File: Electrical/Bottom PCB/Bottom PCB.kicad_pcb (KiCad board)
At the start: 2 copper layers, 100 x 80 mm, 39 parts, among them J1 Steper1, J10 Servo4, J2 Steper2, J3 H Bridge, J4 4 x OP, J6 Servo1, J7 Servo2, J8 Servo3, J9 MainIO, SW1 FL, SW2 FR, U1 ULN2003A, U2 74HC595, U3 QRE1113, U4 TB6612FNG, U5 74HC595, U6 QRE1113, U7 QRE1113, U8 QRE1113

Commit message: updates
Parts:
- moved J1 3.70 mm to (126.0, 111.0)
- moved U1 3.42 mm to (144.0, 119.5)
- moved J2 2.97 mm to (130.0, 111.0)
- moved J6 2.23 mm to (131.5, 75.2)
- moved J10 1.70 mm to (124.0, 75.2)
- moved J7 0.92 mm to (129.0, 75.2)
- moved J8 0.39 mm to (126.5, 75.2)
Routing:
- net Servo4: track 37.6 -> 0.00 mm
- net Servo2: track 32.7 -> 2.00 mm
- net Servo1: track 30.3 -> 0.00 mm
- net +5V: track 142.1 -> 117.3 mm
- net Servo3: track 24.1 -> 0.00 mm
- net DATA: track 20.3 -> 2.14 mm
- net SRCLK: track 37.0 -> 19.8 mm
- net RCLK: track 35.3 -> 22.0 mm
- net OpML: track 102.5 -> 89.5 mm
- net OpFR: track 103.4 -> 91.6 mm
- net Net-(J2-Pad5): track 26.6 -> 28.7 mm
- net Net-(J1-Pad4): track 28.2 -> 26.7 mm
- net Net-(J1-Pad3): track 24.7 -> 23.3 mm
- net Net-(J1-Pad5): track 31.6 -> 30.2 mm
- net Net-(J1-Pad2): track 20.7 -> 19.6 mm
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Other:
- outline, holes or cut-outs redrawn

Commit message: small update
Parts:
- added C1: 100pF, Capacitor_SMD:C_1206_3216Metric_Pad1.42x1.75mm_HandSolder, B.Cu at (145.7, 56.8)
- added C10: 10uF, Capacitor_SMD:C_1206_3216Metric_Pad1.42x1.75mm_HandSolder, B.Cu at (139.0, 62.8)
- added C11: 100pF, Capacitor_SMD:C_1206_3216Metric_Pad1.42x1.75mm_HandSolder, B.Cu at (168.0, 86.2)
- added C12: 10uF, Capacitor_SMD:C_1206_3216Metric_Pad1.42x1.75mm_HandSolder, B.Cu at (168.0, 92.5)
- added C14: 100pF, Capacitor_SMD:C_1206_3216Metric_Pad1.42x1.75mm_HandSolder, B.Cu at (153.8, 67.0)
- added C2: 100pF, Capacitor_SMD:C_1206_3216Metric_Pad1.42x1.75mm_HandSolder, B.Cu at (139.0, 57.2)
- added C3: 10uF, Capacitor_SMD:C_1206_3216Metric_Pad1.42x1.75mm_HandSolder, B.Cu at (145.8, 62.2)
- added C4: 100pF, Capacitor_SMD:C_1206_3216Metric_Pad1.42x1.75mm_HandSolder, B.Cu at (139.3, 68.2)
- added C6: 10uF, Capacitor_SMD:C_1206_3216Metric_Pad1.42x1.75mm_HandSolder, B.Cu at (162.0, 92.5)
- added C7: 100pF, Capacitor_SMD:C_1206_3216Metric_Pad1.42x1.75mm_HandSolder, B.Cu at (145.5, 67.8)
- added C8: 10uF, Capacitor_SMD:C_1206_3216Metric_Pad1.42x1.75mm_HandSolder, B.Cu at (154.0, 61.5)
- added C9: 100pF, Capacitor_SMD:C_1206_3216Metric_Pad1.42x1.75mm_HandSolder, F.Cu at (127.7, 69.5)
- C13: renamed from C2; value 10pF -> 100pF; footprint Capacitor_SMD:C_1210_3225Metric_Pad1.42x2.65mm_HandSolder -> Capacitor_SMD:C_1206_3216Metric_Pad1.42x1.75mm_HandSolder
- C15: renamed from C3; value 10pF -> 100pF; footprint Capacitor_SMD:C_1210_3225Metric_Pad1.42x2.65mm_HandSolder -> Capacitor_SMD:C_1206_3216Metric_Pad1.42x1.75mm_HandSolder
- C16: renamed from C4; value 10pF -> 100pF
- C17: renamed from C5; value 10pF -> 100pF; footprint Capacitor_SMD:C_1210_3225Metric_Pad1.42x2.65mm_HandSolder -> Capacitor_SMD:C_1206_3216Metric_Pad1.42x1.75mm_HandSolder
- C5: renamed from C1; value 10pF -> 100pF; footprint Capacitor_SMD:C_1210_3225Metric_Pad1.42x2.65mm_HandSolder -> Capacitor_SMD:C_1206_3216Metric_Pad1.42x1.75mm_HandSolder
- J8: renamed from J9; footprint Connector_PinHeader_2.54mm:PinHeader_1x08_P2.54mm_Vertical -> Connector_PinHeader_2.54mm:PinHeader_1x06_P2.54mm_Vertical
- R1, R10, R11, R12, R2, R3, R4, R5, R6, R7, R8, R9: footprint Resistor_SMD:R_1210_3225Metric_Pad1.42x2.65mm_HandSolder -> Resistor_SMD:R_1206_3216Metric_Pad1.42x1.75mm_HandSolder
- moved Logo1 8.31 mm to (152.8, 89.8)
- moved R2 7.17 mm to (156.0, 92.5), turned to 0 degrees
- moved R3 4.13 mm to (114.0, 108.5)
- moved J8 3.25 mm to (159.1, 77.5)
- moved C5 2.09 mm to (162.0, 86.2)
- moved R1 2.08 mm to (156.0, 86.2)
- moved U2 2.01 mm to (141.2, 105.4)
- moved SW2 0.37 mm to (119.0, 70.8)
- moved SW1 0.27 mm to (119.0, 108.5)
- renumbered J6 to J5, J7 to J6, J8 to J7, J10 to J9
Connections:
- A1 pad 10: Servo4 -> Servo3
- A1 pad 11: Servo3 -> Servo4
- A1 pad 19: Servo2 -> Net-(A1-Pad19)
- A1 pad 20: Servo1 -> Net-(A1-Pad20)
- A1 pad 5: Net-(A1-Pad5) -> Servo1
- A1 pad 6: Net-(A1-Pad6) -> Servo2
- J8 pad 2: +BATT -> +5V
- J8 pad 3: +5V -> GND
- J8 pad 4: +5V -> RX
- J8 pad 5: GND -> TX
- J8 pad 6: RX -> GND
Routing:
- net +5V: track 117.3 -> 12.0 mm, vias 9 -> 0
- net OpFR: track 91.6 -> 0.00 mm, vias 2 -> 0
- net OpML: track 89.5 -> 0.00 mm, vias 3 -> 0
- net OpMR: track 61.2 -> 0.00 mm, vias 2 -> 0
- net OpFL: track 56.4 -> 0.00 mm
- net Sonar: track 34.3 -> 0.00 mm
- net SwFL: track 32.1 -> 0.00 mm
- net M1PWM: track 30.6 -> 0.00 mm, vias 1 -> 0
- net Net-(J1-Pad5): track 30.2 -> 0.00 mm
- net GND: track 29.9 -> 0.00 mm, vias 2 -> 0
- net SwFR: track 29.3 -> 0.00 mm
- net Net-(J2-Pad5): track 28.7 -> 0.00 mm
- net M2PWM: track 27.9 -> 0.00 mm, vias 1 -> 0
- net Net-(J1-Pad4): track 26.7 -> 0.00 mm
- net Net-(J2-Pad4): track 25.0 -> 0.00 mm
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
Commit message: Update Bottom PCB.kicad_pcb
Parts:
- C16: footprint Capacitor_SMD:C_1210_3225Metric_Pad1.42x2.65mm_HandSolder -> Capacitor_SMD:C_1206_3216Metric_Pad1.42x1.75mm_HandSolder
- C9: moved to B.Cu
- moved C17 30.6 mm to (110.2, 82.5), turned to 270 degrees
- moved C9 7.45 mm to (131.8, 63.2)
- moved C7 5.33 mm to (141.5, 71.3), turned to 90 degrees
- moved C4 4.07 mm to (136.5, 71.2), turned to 90 degrees
- moved C15 2.05 mm to (121.2, 53.3), turned to 90 degrees
- moved U8 0.74 mm to (103.6, 80.8)
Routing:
- net BatV: track 17.6 -> 0.00 mm
- net +BATT: track 16.6 -> 0.00 mm
- net +5V: track 12.0 -> 0.00 mm
- net RX: track 5.63 -> 0.00 mm
- net TX: track 5.63 -> 0.00 mm

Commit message: Changed IR sensors to allow for passive measurments
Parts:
- removed J4: 4 x OP, Connector_PinHeader_2.54mm:PinHeader_1x04_P2.54mm_Vertical
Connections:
- R11 pad 2: +5V -> IR
- R5 pad 2: +5V -> IR
- R7 pad 2: +5V -> IR
- R9 pad 2: +5V -> IR
- U5 pad 4: Net-(J4-Pad1) -> IR

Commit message: Adding 9 DoF IMU
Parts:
- added U9: MPU-9250, Sensor_Motion:InvenSense_QFN-24_3x3mm_P0.4mm, F.Cu at (148.0, 89.5)
- moved Logo1 0.35 mm to (152.5, 89.5)
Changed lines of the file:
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@@
     (tracks 0)
     (zones 0)
-    (modules 50)
-    (nets 67)
+    (modules 51)
+    (nets 81)
   )
   (page A4)
@@
     (0 F.Cu signal)
     (31 B.Cu signal)
-    (32 B.Adhes user hide)
-    (33 F.Adhes user hide)
+    (32 B.Adhes user)
+    (33 F.Adhes user)
     (34 B.Paste user)
-    (35 F.Paste user hide)
+    (35 F.Paste user)
     (36 B.SilkS user)
-    (37 F.SilkS user hide)
+    (37 F.SilkS user)
     (38 B.Mask user)
-    (39 F.Mask user hide)
-    (40 Dwgs.User user hide)
-    (41 Cmts.User user hide)
-    (42 Eco1.User user hide)
-    (43 Eco2.User user hide)
+    (39 F.Mask user)
+    (40 Dwgs.User user)
+    (41 Cmts.User user)
+    (42 Eco1.User user)
+    (43 Eco2.User user)
     (44 Edge.Cuts user)
-    (45 Margin user hide)
+    (45 Margin user)
     (46 B.CrtYd user)
-    (47 F.CrtYd user hide)
+    (47 F.CrtYd user)
     (48 B.Fab user)
-    (49 F.Fab user hide)
+    (49 F.Fab user)
   )
   (setup
@@
   (net 65 "Net-(U5-Pad6)")
   (net 66 "Net-(U5-Pad5)")
+  (net 67 "Net-(U9-Pad24)")
+  (net 68 "Net-(U9-Pad23)")
+  (net 69 "Net-(U9-Pad22)")
+  (net 70 "Net-(U9-Pad21)")
+  (net 71 "Net-(U9-Pad20)")
+  (net 72 "Net-(U9-Pad18)")
+  (net 73 "Net-(U9-Pad13)")
+  (net 74 "Net-(U9-Pad12)")
+  (net 75 "Net-(U9-Pad11)")
+  (net 76 "Net-(U9-Pad10)")
+  (net 77 "Net-(U9-Pad9)")
+  (net 78 "Net-(U9-Pad8)")
+  (net 79 "Net-(U9-Pad7)")
+  (net 80 "Net-(U9-Pad1)")
   (net_class Default "This is the default net class."
     (clearance 0.2)
@@
     (add_net "Net-(U5-Pad7)")
     (add_net "Net-(U5-Pad9)")
+    (add_net "Net-(U9-Pad1)")
+    (add_net "Net-(U9-Pad10)")
+    (add_net "Net-(U9-Pad11)")
+    (add_net "Net-(U9-Pad12)")
+    (add_net "Net-(U9-Pad13)")
+    (add_net "Net-(U9-Pad18)")
+    (add_net "Net-(U9-Pad20)")
+    (add_net "Net-(U9-Pad21)")
+    (add_net "Net-(U9-Pad22)")
+    (add_net "Net-(U9-Pad23)")
+    (add_net "Net-(U9-Pad24)")
+    (add_net "Net-(U9-Pad7)")
+    (add_net "Net-(U9-Pad8)")
+    (add_net "Net-(U9-Pad9)")
     (add_net OpFL)
     (add_net OpFR)
@@
     (add_net BatV)
     (add_net GND)
+  )
+  (module Sensor_Motion:InvenSense_QFN-24_3x3mm_P0.4mm (layer F.Cu)
+    (at 148 89.5)
+    (descr "24-Lead Plastic QFN (3mm x 3mm); Pitch 0.4mm; EP 1.7x1.54mm; for InvenSense motion sensors; keepout area marked (Package see: https://store.invensense.com/datasheets/invensense/MPU9250REV1.0.pdf; See also https://www.invensense.com/wp-content/uploads/2015/02/InvenSense-MEMS-Handling.pdf)")
+    (tags "QFN 0.4")
+    (attr smd)
+    (fp_text reference U9 (at 0 -3.25) (layer F.SilkS)
+      (effects (font (size 1 1) (thickness 0.15)))
+    )
+    (fp_text value MPU-9250 (at 0 3.25) (layer F.Fab)
+      (effects (font (size 1 1) (thickness 0.15)))
+    )
+    (fp_text user Component (at 0 0.55) (layer Cmts.User)
+      (effects (font (size 0.2 0.2) (thickness 0.04)))
+    )
+    (fp_text user "Directly Below" (at 0 0.25) (layer Cmts.User)
+      (effects (font (size 0.2 0.2) (thickness 0.04)))
+    )
+    (fp_text user "No Copper" (at 0 -0.1) (layer Cmts.User)
+      (effects (font (size 0.2 0.2) (thickness 0.04)))
+    )
+    (fp_text user KEEPOUT (at 0 -0.5) (layer Cmts.User)
+      (effects (font (size 0.2 0.2) (thickness 0.04)))
+    )
+    (fp_line (start -0.535 -0.795) (end -0.875 -0.455) (layer Dwgs.User) (width 0.05))
+    (fp_line (start -0.035 -0.795) (end -0.875 0.045) (layer Dwgs.User) (width 0.05))
+    (fp_line (start 0.465 -0.795) (end -0.875 0.545) (layer Dwgs.User) (width 0.05))
+    (fp_line (start 0.875 -0.705) (end -0.625 0.795) (layer Dwgs.User) (width 0.05))
+    (fp_line (start 0.875 -0.205) (end -0.125 0.795) (layer Dwgs.User) (width 0.05))
+    (fp_line (start 0.875 0.295) (end 0.375 0.795) (layer Dwgs.User) (width 0.05))
+    (fp_line (start 0.875 -0.795) (end 0.875 0.795) (layer Dwgs.User) (width 0.05))
+    (fp_line (start -0.875 0.795) (end 0.875 0.795) (layer Dwgs.User) (width 0.05))
+    (fp_line (start -0.875 -0.795) (end -0.875 0.795) (layer Dwgs.User) (width 0.05))
+    (fp_line (start -0.875 -0.795) (end 0.875 -0.795) (layer Dwgs.User) (width 0.05))
+    (fp_line (start -1.6 -1.6) (end -1.2 -1.6) (layer F.SilkS) (width 0.15))
+    (fp_line (start 1.6 -1.6) (end 1.2 -1.6) (layer F.SilkS) (width 0.15))
+    (fp_line (start 1.6 -1.6) (end 1.6 -1.2) (layer F.SilkS) (width 0.15))
+    (fp_line (start 1.6 1.6) (end 1.2 1.6) (layer F.SilkS) (width 0.15))
+    (fp_line (start 1.6 1.6) (end 1.6 1.2) (layer F.SilkS) (width 0.15))
+    (fp_line (start -1.6 1.6) (end -1.2 1.6) (layer F.SilkS) (width 0.15))
+    (fp_line (start -1.6 1.6) (end -1.6 1.2) (layer F.SilkS) (width 0.15))
+    (fp_line (start -2.05 -2.05) (end 2.05 -2.05) (layer F.CrtYd) (width 0.05))
+    (fp_line (start -2.05 2.05) (end -2.05 -2.05) (layer F.CrtYd) (width 0.05))
+    (fp_line (start 2.05 2.05) (end -2.05 2.05) (layer F.CrtYd) (width 0.05))
+    (fp_line (start 2.05 -2.05) (end 2.05 2.05) (layer F.CrtYd) (width 0.05))
+    (fp_line (start -1.5 -0.5) (end -0.5 -1.5) (layer F.Fab) (width 0.15))
+    (fp_line (start -1.5 1.5) (end -1.5 -0.5) (layer F.Fab) (width 0.15))
+    (fp_line (start 1.5 1.5) (end -1.5 1.5) (layer F.Fab) (width 0.15))
+    (fp_line (start 1.5 -1.5) (end 1.5 1.5) (layer F.Fab) (width 0.15))
+    (fp_line (start -0.5 -1.5) (end 1.5 -1.5) (layer F.Fab) (width 0.15))
+    (fp_text user %R (at 0 0) (layer F.Fab)
+      (effects (font (size 0.7 0.7) (thickness 0.105)))
+    )
+    (pad 24 smd roundrect (at -1 -1.5 90) (size 0.55 0.2) (layers F.Cu F.Paste F.Mask) (roundrect_rratio 0.25)
+      (net 67 "Net-(U9-Pad24)"))
+    (pad 23 smd roundrect (at -0.6 -1.5 90) (size 0.55 0.2) (layers F.Cu F.Paste F.Mask) (roundrect_rratio 0.25)
+      (net 68 "Net-(U9-Pad23)"))
+    (pad 22 smd roundrect (at -0.2 -1.5 90) (size 0.55 0.2) (layers F.Cu F.Paste F.Mask) (roundrect_rratio 0.25)
+      (net 69 "Net-(U9-Pad22)"))
+    (pad 21 smd roundrect (at 0.2 -1.5 90) (size 0.55 0.2) (layers F.Cu F.Paste F.Mask) (roundrect_rratio 0.25)
+      (net 70 "Net-(U9-Pad21)"))
+    (pad 20 smd roundrect (at 0.6 -1.5 90) (size 0.55 0.2) (layers F.Cu F.Paste F.Mask) (roundrect_rratio 0.25)
+      (net 71 "Net-(U9-Pad20)"))
+    (pad 19 smd roundrect (at 1 -1.5 90) (size 0.55 0.2) (layers F.Cu F.Paste F.Mask) (roundrect_rratio 0.25))
+    (pad 18 smd roundrect (at 1.5 -1) (size 0.55 0.2) (layers F.Cu F.Paste F.Mask) (roundrect_rratio 0.25)
+      (net 72 "Net-(U9-Pad18)"))
+    (pad 17 smd roundrect (at 1.5 -0.6) (size 0.55 0.2) (layers F.Cu F.Paste F.Mask) (roundrect_rratio 0.25))
+    (pad 16 smd roundrect (at 1.5 -0.2) (size 0.55 0.2) (layers F.Cu F.Paste F.Mask) (roundrect_rratio 0.25))
+    (pad 15 smd roundrect (at 1.5 0.2) (size 0.55 0.2) (layers F.Cu F.Paste F.Mask) (roundrect_rratio 0.25))
+    (pad 14 smd roundrect (at 1.5 0.6) (size 0.55 0.2) (layers F.Cu F.Paste F.Mask) (roundrect_rratio 0.25))
+    (pad 13 smd roundrect (at 1.5 1) (size 0.55 0.2) (layers F.Cu F.Paste F.Mask) (roundrect_rratio 0.25)
+      (net 73 "Net-(U9-Pad13)"))
+    (pad 12 smd roundrect (at 1 1.5 90) (size 0.55 0.2) (layers F.Cu F.Paste F.Mask) (roundrect_rratio 0.25)
+      (net 74 "Net-(U9-Pad12)"))
+    (pad 11 smd roundrect (at 0.6 1.5 90) (size 0.55 0.2) (layers F.Cu F.Paste F.Mask) (roundrect_rratio 0.25)
+      (net 75 "Net-(U9-Pad11)"))
+    (pad 10 smd roundrect (at 0.2 1.5 90) (size 0.55 0.2) (layers F.Cu F.Paste F.Mask) (roundrect_rratio 0.25)
+      (net 76 "Net-(U9-Pad10)"))
+    (pad 9 smd roundrect (at -0.2 1.5 90) (size 0.55 0.2) (layers F.Cu F.Paste F.Mask) (roundrect_rratio 0.25)
+      (net 77 "Net-(U9-Pad9)"))
+    (pad 8 smd roundrect (at -0.6 1.5 90) (size 0.55 0.2) (layers F.Cu F.Paste F.Mask) (roundrect_rratio 0.25)
+      (net 78 "Net-(U9-Pad8)"))
+    (pad 7 smd roundrect (at -1 1.5 90) (size 0.55 0.2) (layers F.Cu F.Paste F.Mask) (roundrect_rratio 0.25)
+      (net 79 "Net-(U9-Pad7)"))
+    (pad 6 smd roundrect (at -1.5 1) (size 0.55 0.2) (layers F.Cu F.Paste F.Mask) (roundrect_rratio 0.25))
+    (pad 5 smd roundrect (at -1.5 0.6) (size 0.55 0.2) (layers F.Cu F.Paste F.Mask) (roundrect_rratio 0.25))
+    (pad 4 smd roundrect (at -1.5 0.2) (size 0.55 0.2) (layers F.Cu F.Paste F.Mask) (roundrect_rratio 0.25))
+    (pad 3 smd roundrect (at -1.5 -0.2) (size 0.55 0.2) (layers F.Cu F.Paste F.Mask) (roundrect_rratio 0.25))
+    (pad 2 smd roundrect (at -1.5 -0.6) (size 0.55 0.2) (layers F.Cu F.Paste F.Mask) (roundrect_rratio 0.25))
+    (pad 1 smd roundrect (at -1.5 -1) (size 0.55 0.2) (layers F.Cu F.Paste F.Mask) (roundrect_rratio 0.25)
+      (net 80 "Net-(U9-Pad1)"))
+    (model ${KISYS3DMOD}/Package_DFN_QFN.3dshapes/QFN-24_3x3mm_P0.4mm_EP1.7x1.54mm.wrl
+      (at (xyz 0 0 0))
+      (scale (xyz 1 1 1))
+      (rotate (xyz 0 0 0))
+    )
   )
   (module Capacitor_SMD:C_1206_3216Metric_Pad1.42x1.75mm_HandSolder (layer B.Cu)
@@
   )
   (module "SquashedFly Logo:SquashedFly Logo" (layer F.Cu)
-    (at 152.75 89.75)
+    (at 152.5 89.5)
     (fp_text reference Logo1 (at 0 4.71) (layer F.SilkS) hide
       (effects (font (size 1 1) (thickness 0.15)))

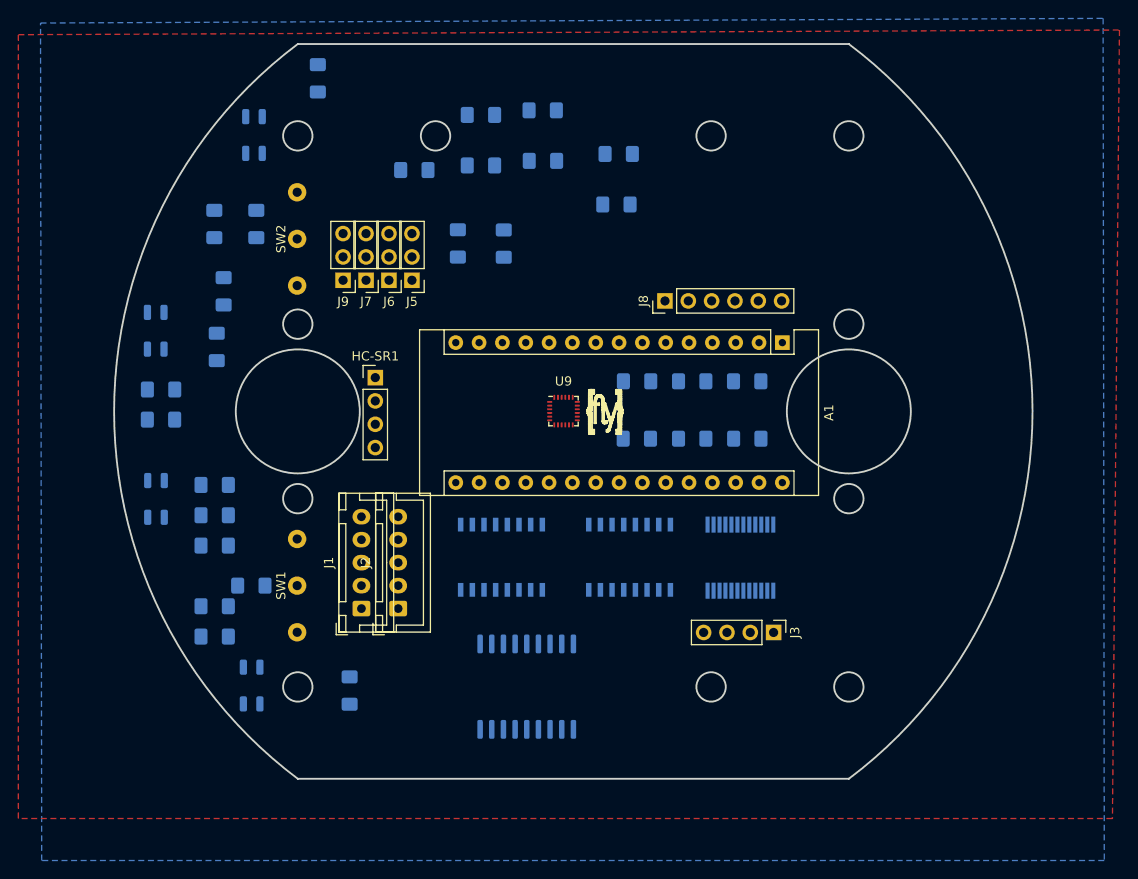
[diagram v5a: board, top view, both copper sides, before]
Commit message: Change MCU
swap arduino to ESP32-Wroom

https://www.mouser.co.uk/ProductDetail/Espressif/ESP32-WROVER/?qs=chTDxNqvsynCfB3ibKeA%252bA%3D%3D

Mouser No: 356-ESP32-WROVER
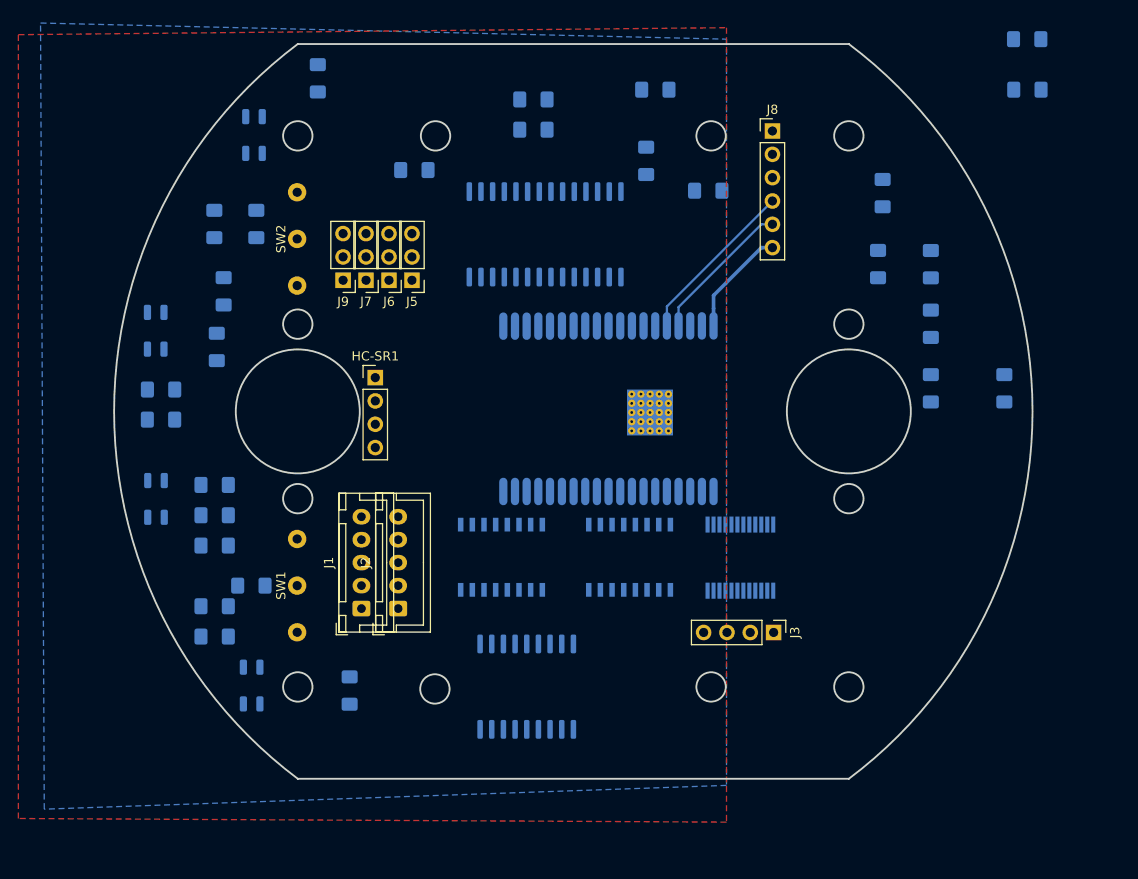
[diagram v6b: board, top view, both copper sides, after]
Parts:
- removed A1: Arduino_Nano_v3.x, Module:Arduino_Nano
- removed C11, C5: 100pF, Capacitor_SMD:C_1206_3216Metric_Pad1.42x1.75mm_HandSolder
- removed C12: 10uF, Capacitor_SMD:C_1206_3216Metric_Pad1.42x1.75mm_HandSolder
- added C18: 10uF, Capacitor_SMD:C_1206_3216Metric_Pad1.42x1.75mm_HandSolder, B.Cu at (144.7, 58.9)
- added C19: 100pF, Capacitor_SMD:C_1206_3216Metric_Pad1.42x1.75mm_HandSolder, B.Cu at (144.7, 55.6)
- added U10: MCP23017_SO, Package_SO:SOIC-28W_7.5x17.9mm_P1.27mm, B.Cu at (146.0, 70.2)
- Logo1: moved to B.Cu
- R1: value 10k -> 22k
- U9: value MPU-9250 -> ESP32-WROVER; footprint Sensor_Motion:InvenSense_QFN-24_3x3mm_P0.4mm -> esp32-wrover:ESP32-WROVER; moved to B.Cu
- moved C1 53.3 mm to (198.5, 49.0)
- moved C3 53.3 mm to (198.5, 54.5)
- moved C14 46.7 mm to (196.0, 87.0), turned to 270 degrees
- moved C8 42.5 mm to (188.0, 87.0), turned to 270 degrees
- moved C7 41.6 mm to (182.8, 65.8)
- moved Logo1 37.7 mm to (180.8, 114.5), turned to 270 degrees
- moved R2 37.2 mm to (188.0, 73.5), turned to 270 degrees
- moved R1 32.6 mm to (188.0, 80.0), turned to 270 degrees
- moved C6 27.8 mm to (182.2, 73.5), turned to 90 degrees
- moved C10 24.9 mm to (163.8, 65.5)
- moved C4 22.4 mm to (157.0, 62.2)
- moved J8 21.9 mm to (170.8, 59.0), turned to 0 degrees
- moved C2 19.2 mm to (158.0, 54.5)
- moved U9 17.3 mm to (165.2, 89.2), turned to 90 degrees
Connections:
- U9 pad 1: Net-(U9-Pad1) -> GND
- U9 pad 14: (no net) -> Net-(U9-Pad14)
- U9 pad 15: (no net) -> GND
- U9 pad 16: (no net) -> Net-(U9-Pad16)
- U9 pad 17: (no net) -> Net-(U9-Pad17)
- U9 pad 19: (no net) -> Net-(U9-Pad19)
- U9 pad 2: (no net) -> +3V3
- U9 pad 3: (no net) -> Net-(U9-Pad3)
- U9 pad 4: (no net) -> Net-(U9-Pad4)
- U9 pad 5: (no net) -> Net-(U9-Pad5)
- U9 pad 6: (no net) -> Net-(U9-Pad6)
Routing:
- net RX: track 0.00 -> 18.4 mm
- net TX: track 0.00 -> 16.0 mm
- net GND: track 0.00 -> 11.9 mm
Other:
- outline, holes or cut-outs redrawn
